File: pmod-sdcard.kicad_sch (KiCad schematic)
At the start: 4 parts, among them J1 PMOD_Peripheral_Conn_02x06, J2 Micro_SD_Card

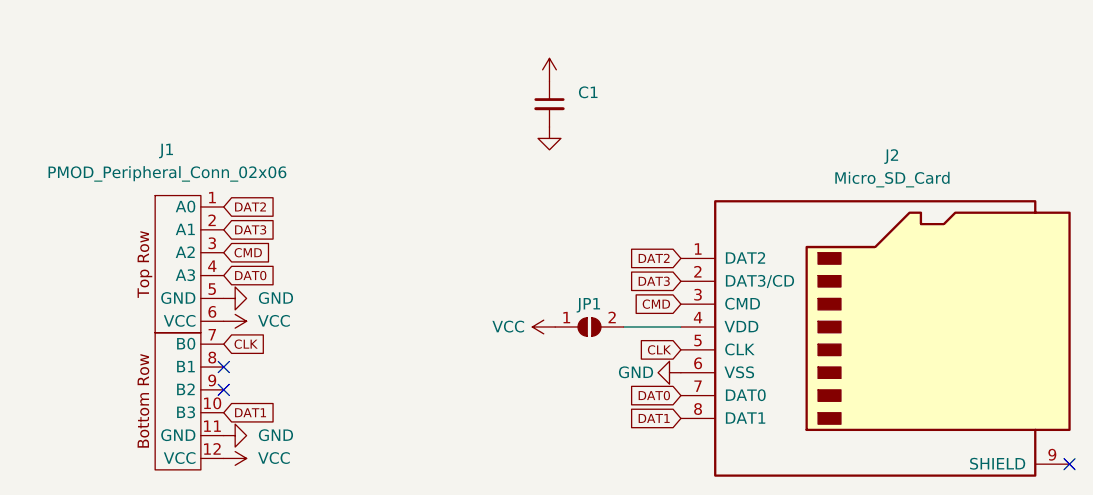
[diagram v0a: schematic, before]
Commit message: Add series resistors for signal lines
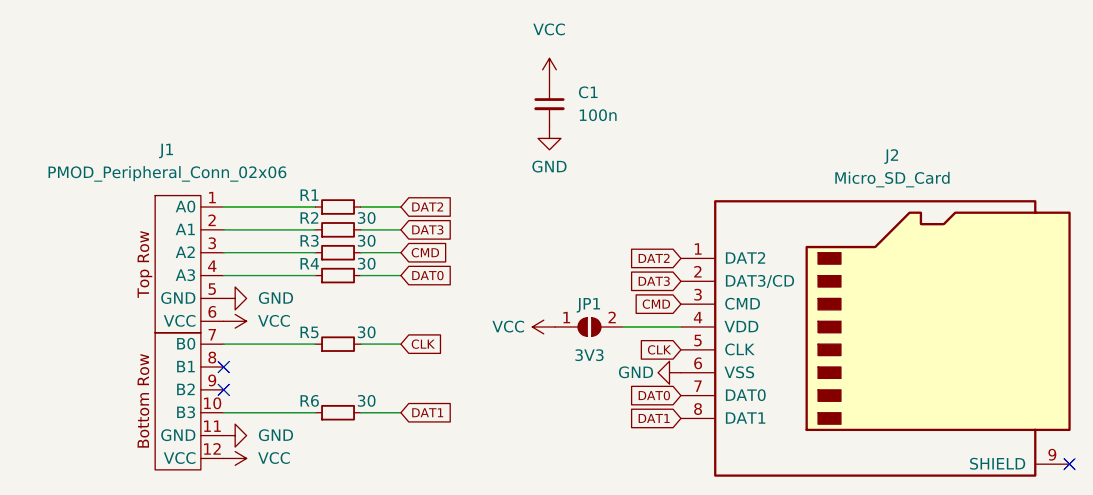
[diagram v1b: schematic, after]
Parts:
- added R1: (no value), symbol Device:R_Small
- added R2, R3, R4, R5, R6: 30, symbol Device:R_Small
- C1: value (none) -> 100n; footprint (none) -> Capacitor_SMD:C_0603_1608Metric_Pad1.08x0.95mm_HandSolder
- JP1: value (none) -> 3V3; footprint (none) -> Jumper:SolderJumper-2_P1.3mm_Open_RoundedPad1.0x1.5mm
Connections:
- net CLK: now also R5.2; no longer J1.7 (B0)
- net CMD: now also R3.2; no longer J1.3 (A2)
- net DAT0: now also R4.2; no longer J1.4 (A3)
- net DAT1: now also R6.2; no longer J1.10 (B3)
- net DAT2: now also R1.2; no longer J1.1 (A0)
- net DAT3: now also R2.2; no longer J1.2 (A1)
- new net: J1.2 (A1), R2.1
- new net: J1.3 (A2), R3.1
- new net: J1.1 (A0), R1.1
- new net: J1.10 (B3), R6.1
- new net: J1.4 (A3), R4.1
- new net: J1.7 (B0), R5.1
